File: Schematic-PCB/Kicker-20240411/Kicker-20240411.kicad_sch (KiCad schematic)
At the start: 23 parts, among them J1 Conn_01x02_Pin, J2 Conn_01x05_Pin, J3 Conn_01x02_Pin, Q1 NMOS, Q2 NMOS, U1 TSSP58P38, U2 TSSP58P38

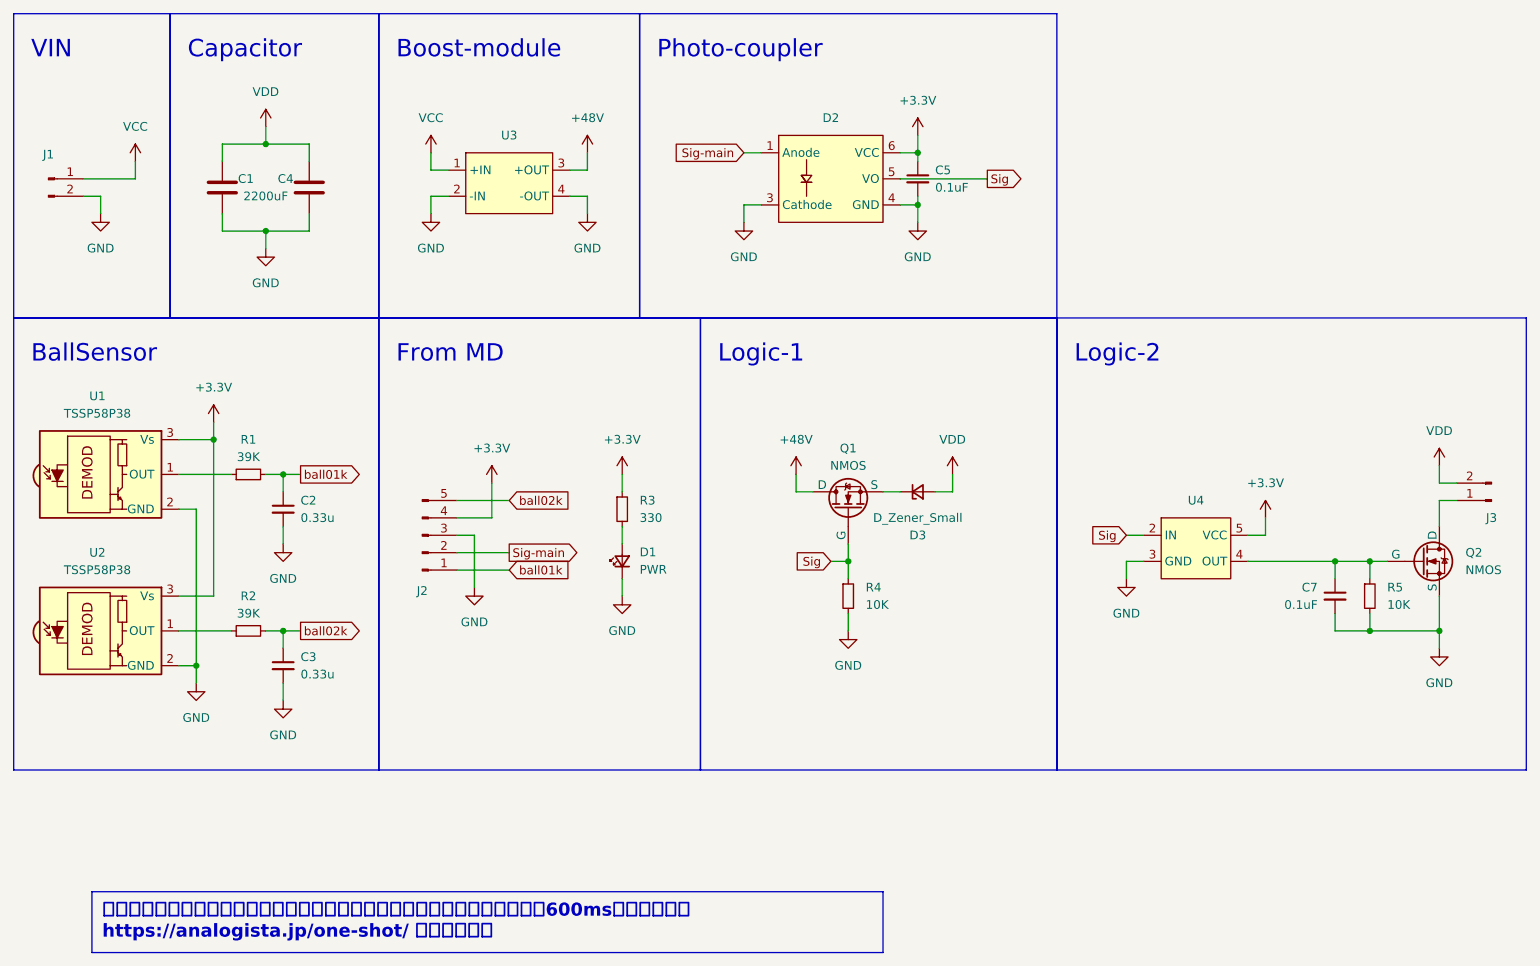
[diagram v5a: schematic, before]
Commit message: update: キッカー基板の回路図を修正した
ツェナーダイオードをなくした
+48V-+VDD関連のNchMOSFETのロジックを削除した
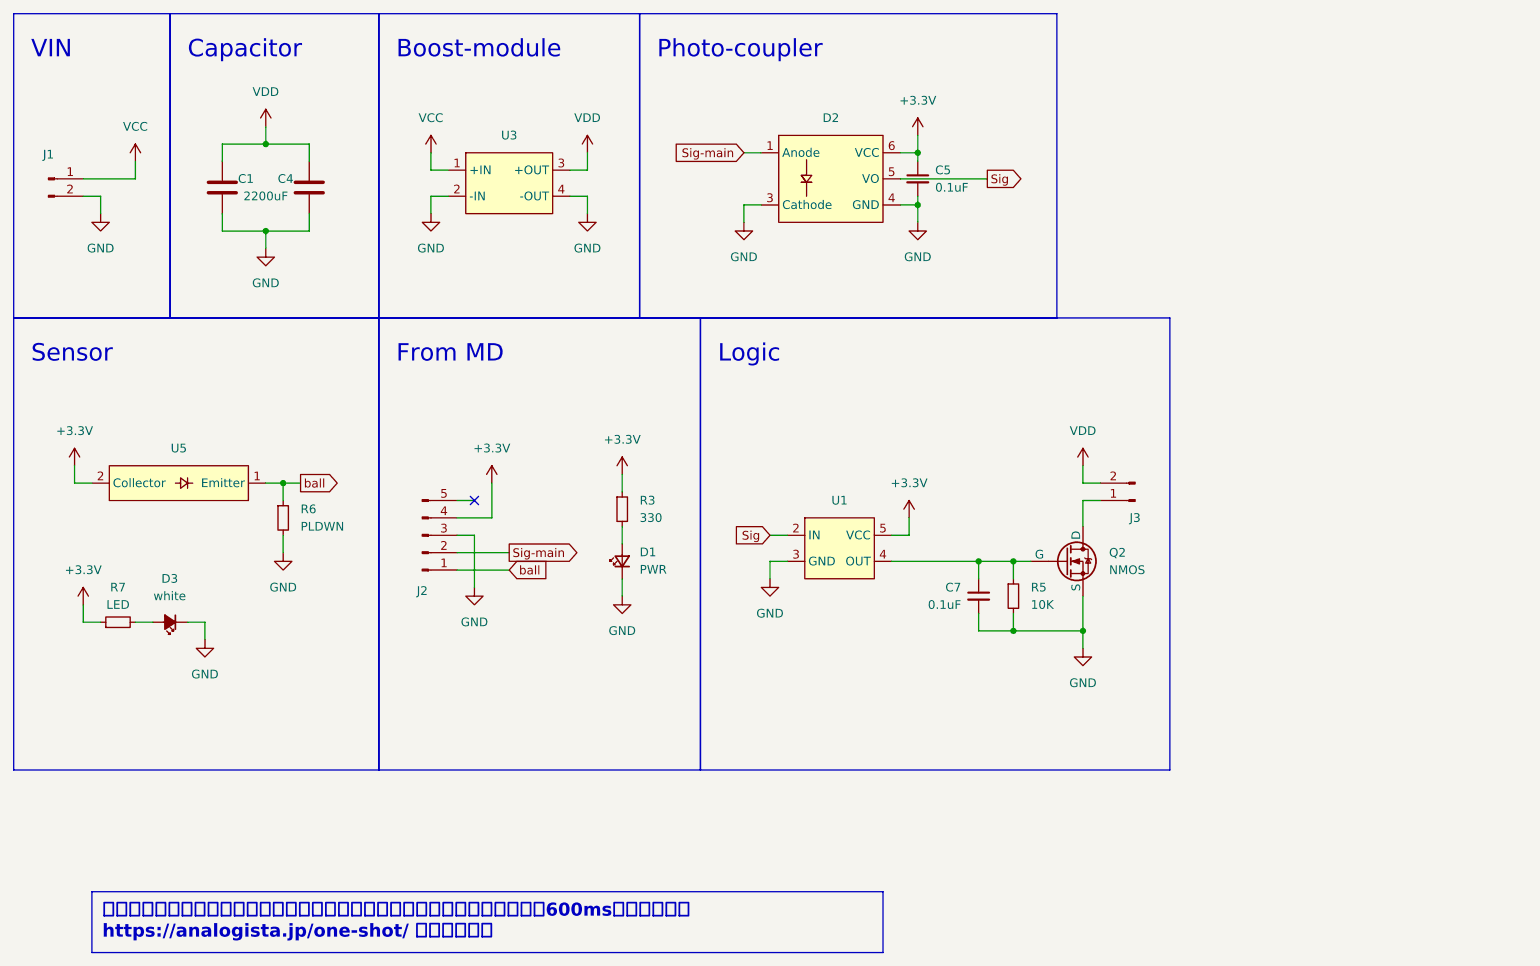
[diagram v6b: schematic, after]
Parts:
- removed C2, C3: 0.33u, Capacitor_SMD:C_0603_1608Metric, symbol Device:C_Small
- removed D3: D_Zener_Small, symbol Device:D_Zener_Small
- removed Q1: NMOS, Package_TO_SOT_SMD:TO-252-2, symbol @2023_KickerAdjust:NMOS
- removed R1, R2: 39K, Resistor_SMD:R_0603_1608Metric, symbol Device:R_Small
- removed R4: 10K, Resistor_SMD:R_0603_1608Metric, symbol Device:R_Small
- removed U1, U2: TSSP58P38, OptoDevice:Vishay_MINICAST-3Pin, symbol Sensor_Proximity:TSSP58P38
- removed U4: ~, Package_TO_SOT_SMD:SOT-23-5, symbol @2024TOINIOT2-Kicker:74AHC1G04W5
- added D3: white, symbol Device:LED_Small_Filled
- added R6: PLDWN, symbol Device:R_Small
- added R7: LED, symbol Device:R_Small
- added U1: ~, Package_TO_SOT_SMD:SOT-23-5, symbol @2024-Kicker:74AHC1G04W5
- added U5: ~, @2024TOINIOT2-Line:NJL7502L, symbol @2024-Line:NJL7502L
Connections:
- net +48V is gone; now on net VDD: U3.3 (+OUT)
- net +3.3V: now also R7.1, U1.5 (VCC), U5.2 (Collector)
- net GND: now also D3.1 (K), R6.2, U1.3 (GND)
- net Sig: now also U1.2 (IN)
- net at C7.1, Q2.1 (G), R5.1: now also U1.4 (OUT)
- net ball01k renamed ball
- net ball: now also R6.1, U5.1 (Emitter)
- net ball02k: no longer names the net of J2.5 (Pin_5)
- new net: D3.2 (A), R7.2
- no-connect marks 0 -> 1
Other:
- note added: "Logic"
- note added: "Sensor"
- note removed: "BallSensor"
- note removed: "Logic-1"
- note removed: "Logic-2"
- moved on the sheet: C7, J3, Q2, R5

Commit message: add: ラインセンサ基板ver.004のKiCadプロジェクトを作成した
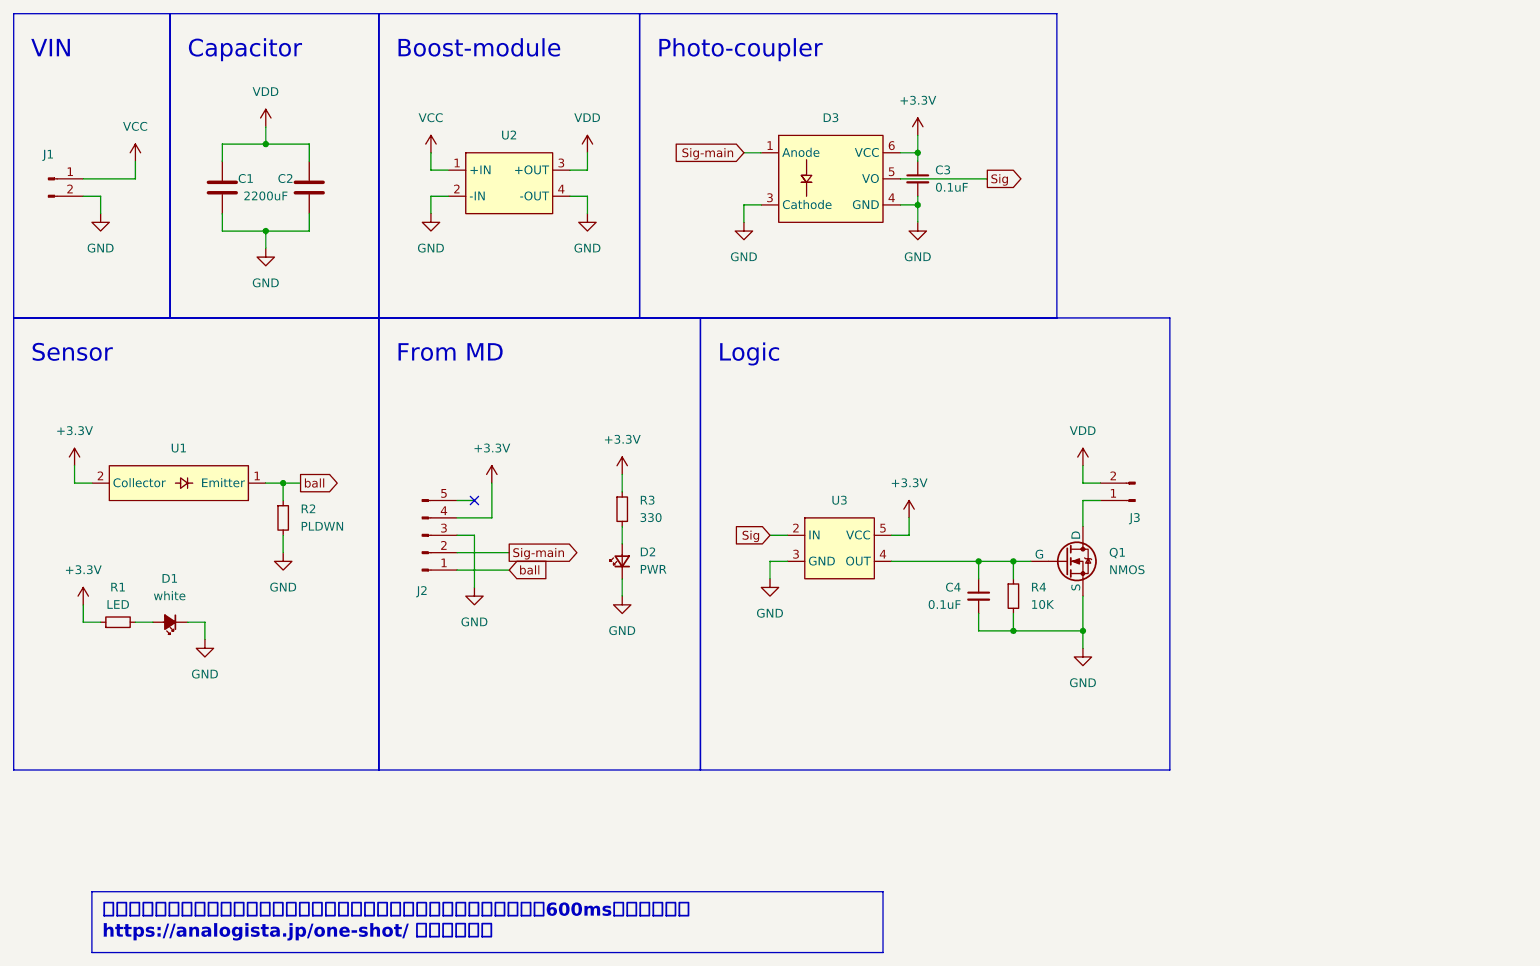
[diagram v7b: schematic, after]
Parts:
- D1: renamed from D3; footprint (none) -> LED_THT:LED_D3.0mm
- R1: renamed from R7; footprint (none) -> Resistor_SMD:R_0603_1608Metric
- R2: renamed from R6; footprint (none) -> Resistor_SMD:R_0603_1608Metric
- renumbered C4 to C2, C5 to C3, C7 to C4, D1 to D2, D2 to D3, Q2 to Q1, R5 to R4, U5 to U1, U3 to U2, U1 to U3
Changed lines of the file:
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@@
 		(dnp no)
 		(fields_autoplaced yes)
-		(property "Reference" "R6"
+		(property "Reference" "R2"
 			(at 54.61 85.09 0)
 			(effects
@@
 			)
 		)
-		(property "Footprint" ""
+		(property "Footprint" "Resistor_SMD:R_0603_1608Metric"
 			(at 52.07 86.36 0)
 			(effects
@@
 			(project "Kicker-20240411"
 				(path "/2edfd9df-91eb-4b22-a740-f92ff97fc327"
-					(reference "R6")
+					(reference "R2")
 					(unit 1)
 				)
@@
 		(dnp no)
 		(fields_autoplaced yes)
-		(property "Reference" "#PWR029"
+		(property "Reference" "#PWR02"
 			(at 22.86 102.87 0)
 			(effects
@@
 			(project "Kicker-20240411"
 				(path "/2edfd9df-91eb-4b22-a740-f92ff97fc327"
-					(reference "#PWR029")
+					(reference "#PWR02")
 					(unit 1)
 				)
@@
 		(dnp no)
 		(fields_autoplaced yes)
-		(property "Reference" "#PWR03"
+		(property "Reference" "#PWR013"
 			(at 96.52 36.83 0)
 			(effects
@@
 			(project "Kicker-20240411"
 				(path "/2edfd9df-91eb-4b22-a740-f92ff97fc327"
-					(reference "#PWR03")
+					(reference "#PWR013")
 					(unit 1)
 				)
@@
 		(dnp no)
 		(fields_autoplaced yes)
-		(property "Reference" "#PWR06"
+		(property "Reference" "#PWR07"
 			(at 49.53 53.34 0)
 			(effects
@@
 			(project "Kicker-20240411"
 				(path "/2edfd9df-91eb-4b22-a740-f92ff97fc327"
-					(reference "#PWR06")
+					(reference "#PWR07")
 					(unit 1)
 				)
@@
 		(dnp no)
 		(fields_autoplaced yes)
-		(property "Reference" "C5"
+		(property "Reference" "C3"
 			(at 147.32 35.5663 0)
 			(effects
@@
 			(project "Kicker-20240411"
 				(path "/2edfd9df-91eb-4b22-a740-f92ff97fc327"
-					(reference "C5")
+					(reference "C3")
 					(unit 1)
 				)
@@
 		(dnp no)
 		(fields_autoplaced yes)
-		(property "Reference" "#PWR024"
+		(property "Reference" "#PWR019"
 			(at 143.51 90.17 0)
 			(effects
@@
 			(project "Kicker-20240411"
 				(path "/2edfd9df-91eb-4b22-a740-f92ff97fc327"
-					(reference "#PWR024")
+					(reference "#PWR019")
 					(unit 1)
 				)
@@
 		(dnp no)
 		(fields_autoplaced yes)
-		(property "Reference" "#PWR028"
+		(property "Reference" "#PWR08"
 			(at 52.07 97.79 0)
 			(effects
@@
 			(project "Kicker-20240411"
 				(path "/2edfd9df-91eb-4b22-a740-f92ff97fc327"
-					(reference "#PWR028")
+					(reference "#PWR08")
 					(unit 1)
 				)
@@
 		(dnp no)
 		(fields_autoplaced yes)
-		(property "Reference" "#PWR026"
+		(property "Reference" "#PWR023"
 			(at 168.91 111.76 0)
 			(effects
@@
 			(project "Kicker-20240411"
 				(path "/2edfd9df-91eb-4b22-a740-f92ff97fc327"
-					(reference "#PWR026")
+					(reference "#PWR023")
 					(unit 1)
 				)
@@
 		(dnp no)
 		(fields_autoplaced yes)
-		(property "Reference" "U1"
+		(property "Reference" "U3"
 			(at 133.35 83.82 0)
 			(effects
@@
 			(project "Kicker-20240411"
 				(path "/2edfd9df-91eb-4b22-a740-f92ff97fc327"
-					(reference "U1")
+					(reference "U3")
 					(unit 1)
 				)
@@
 		(dnp no)
 		(fields_autoplaced yes)
-		(property "Reference" "U5"
+		(property "Reference" "U1"
 			(at 36.83 76.2 0)
 			(effects
@@
 			(project "Kicker-20240411"
 				(path "/2edfd9df-91eb-4b22-a740-f92ff97fc327"
-					(reference "U5")
+					(reference "U1")
 					(unit 1)
 				)
@@
 		(dnp no)
 		(fields_autoplaced yes)
-		(property "Reference" "U3"
+		(property "Reference" "U2"
 			(at 85.09 30.48 0)
 			(effects
@@
 			(project "Kicker-20240411"
 				(path "/2edfd9df-91eb-4b22-a740-f92ff97fc327"
-					(reference "U3")
+					(reference "U2")
 					(unit 1)
 				)
@@
 		(dnp no)
 		(fields_autoplaced yes)
-		(property "Reference" "Q2"
+		(property "Reference" "Q1"
 			(at 172.72 91.44 0)
 			(effects
@@
 			(project "Kicker-20240411"
 				(path "/2edfd9df-91eb-4b22-a740-f92ff97fc327"
-					(reference "Q2")
+					(reference "Q1")
 					(unit 1)
 				)
@@
 		(dnp no)
 		(fields_autoplaced yes)
-		(property "Reference" "D2"
+		(property "Reference" "D3"
 			(at 132.08 27.94 0)
 			(effects
@@
 			(project "Kicker-20240411"
 				(path "/2edfd9df-91eb-4b22-a740-f92ff97fc327"
-					(reference "D2")
+					(reference "D3")
 					(unit 1)
 				)
@@
 		(dnp no)
 		(fields_autoplaced yes)
-		(property "Reference" "R7"
+		(property "Reference" "R1"
 			(at 27.94 96.52 90)
 			(effects
@@
 			)
 		)
-		(property "Footprint" ""
+		(property "Footprint" "Resistor_SMD:R_0603_1608Metric"
 			(at 27.94 101.6 0)
 			(effects
@@
 			(project "Kicker-20240411"
 				(path "/2edfd9df-91eb-4b22-a740-f92ff97fc327"
-					(reference "R7")
+					(reference "R1")
 					(unit 1)
 				)
@@
 		(dnp no)
 		(fields_autoplaced yes)
-		(property "Reference" "D3"
+		(property "Reference" "D1"
 			(at 35.4965 95.25 0)
 			(effects
@@
 			)
 		)
-		(property "Footprint" ""
+		(property "Footprint" "LED_THT:LED_D3.0mm"
 			(at 35.56 101.6 90)
 			(effects
@@
 			(project "Kicker-20240411"
 				(path "/2edfd9df-91eb-4b22-a740-f92ff97fc327"
-					(reference "D3")
+					(reference "D1")
 					(unit 1)
 				)
@@
 		(dnp no)
 		(fields_autoplaced yes)
-		(property "Reference" "#PWR05"
+		(property "Reference" "#PWR06"
 			(at 49.53 33.02 0)
 			(effects
@@
 			(project "Kicker-20240411"
 				(path "/2edfd9df-91eb-4b22-a740-f92ff97fc327"
-					(reference "#PWR05")
+					(reference "#PWR06")
 					(unit 1)
 				)
@@
 		(on_board yes)
 		(dnp no)
-		(property "Reference" "C7"
+		(property "Reference" "C4"
 			(at 151.13 96.5263 0)
 			(effects
@@
 			(project "Kicker-20240411"
 				(path "/2edfd9df-91eb-4b22-a740-f92ff97fc327"
-					(reference "C7")
+					(reference "C4")
 					(unit 1)
 				)
@@
 		(dnp no)
 		(fields_autoplaced yes)
-		(property "Reference" "#PWR027"
+		(property "Reference" "#PWR01"
 			(at 21.59 82.55 0)
 			(effects
@@
 			(project "Kicker-20240411"
 				(path "/2edfd9df-91eb-4b22-a740-f92ff97fc327"
-					(reference "#PWR027")
+					(reference "#PWR01")
 					(unit 1)
 				)
@@
 		(dnp no)
 		(fields_autoplaced yes)
-		(property "Reference" "#PWR030"
+		(property "Reference" "#PWR05"
 			(at 40.64 110.49 0)
 			(effects
@@
 			(project "Kicker-20240411"
 				(path "/2edfd9df-91eb-4b22-a740-f92ff97fc327"
-					(reference "#PWR030")
+					(reference "#PWR05")
 					(unit 1)
 				)
@@
 		(dnp no)
 		(fields_autoplaced yes)
-		(property "Reference" "#PWR01"
+		(property "Reference" "#PWR03"
 			(at 25.4 48.26 0)
 			(effects
@@
 			(project "Kicker-20240411"
 				(path "/2edfd9df-91eb-4b22-a740-f92ff97fc327"
-					(reference "#PWR01")
+					(reference "#PWR03")
 					(unit 1)
 				)
@@
 		(dnp no)
 		(fields_autoplaced yes)
-		(property "Reference" "#PWR02"
+		(property "Reference" "#PWR04"
 			(at 30.48 38.1 0)
 			(effects
@@
 			(project "Kicker-20240411"
 				(path "/2edfd9df-91eb-4b22-a740-f92ff97fc327"
-					(reference "#PWR02")
+					(reference "#PWR04")
 					(unit 1)
 				)
@@
 		(dnp no)
 		(fields_autoplaced yes)
-		(property "Reference" "R5"
+		(property "Reference" "R4"
 			(at 161.29 96.52 0)
 			(effects
@@
 			(project "Kicker-20240411"
 				(path "/2edfd9df-91eb-4b22-a740-f92ff97fc327"
-					(reference "R5")
+					(reference "R4")
 					(unit 1)
 				)
@@
 		(dnp no)
 		(fields_autoplaced yes)
-		(property "Reference" "D1"
+		(property "Reference" "D2"
 			(at 104.14 91.3765 90)
 			(effects
@@
 			(project "Kicker-20240411"
 				(path "/2edfd9df-91eb-4b22-a740-f92ff97fc327"
-					(reference "D1")
+					(reference "D2")
 					(unit 1)
 				)
@@
 		(on_board yes)
 		(dnp no)
-		(property "Reference" "C4"
+		(property "Reference" "C2"
 			(at 53.594 36.83 0)
 			(effects
@@
 			(project "Kicker-20240411"
 				(path "/2edfd9df-91eb-4b22-a740-f92ff97fc327"
-					(reference "C4")
+					(reference "C2")
 					(unit 1)
 				)
@@
 		(dnp no)
 		(fields_autoplaced yes)
-		(property "Reference" "#PWR023"
+		(property "Reference" "#PWR018"
 			(at 123.19 101.6 0)
 			(effects
@@
 			(project "Kicker-20240411"
 				(path "/2edfd9df-91eb-4b22-a740-f92ff97fc327"
-					(reference "#PWR023")
+					(reference "#PWR018")
 					(unit 1)
 				)
@@
 		(dnp no)
 		(fields_autoplaced yes)
-		(property "Reference" "#PWR025"
+		(property "Reference" "#PWR022"
 			(at 168.91 82.55 0)
 			(effects
@@
 			(project "Kicker-20240411"
 				(path "/2edfd9df-91eb-4b22-a740-f92ff97fc327"
-					(reference "#PWR025")
-					(unit 1)
-				)
+					(reference "#PWR022")
+					(unit 1)
+				)
